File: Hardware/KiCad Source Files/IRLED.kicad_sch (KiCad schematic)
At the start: 14 parts

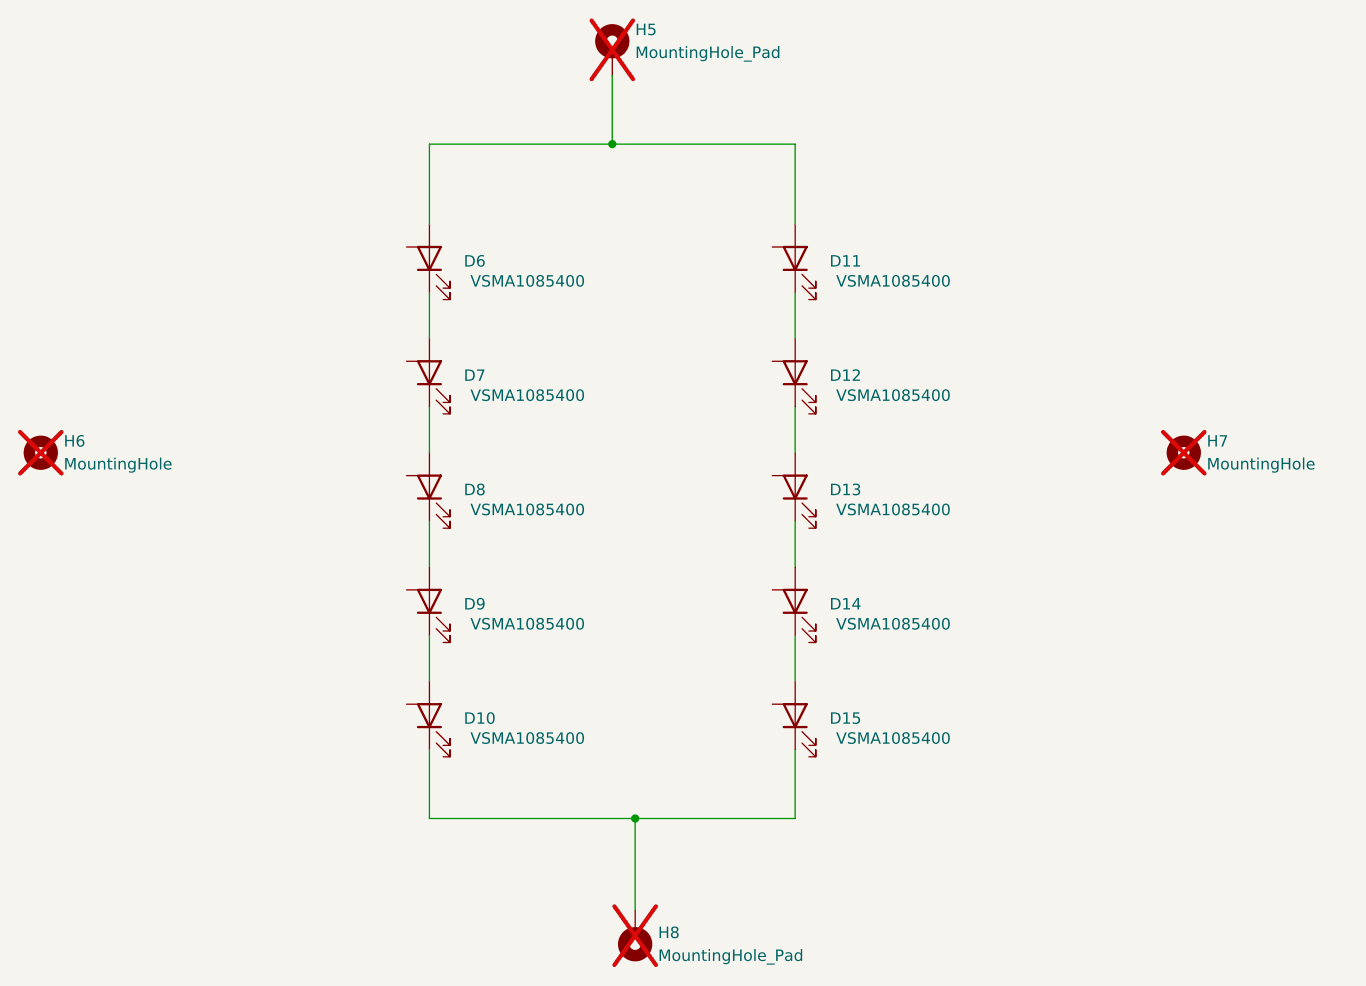
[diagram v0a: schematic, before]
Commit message: V3 connector board: strobe pulse limiter, USB-C fixes, boost protection
Mechanical: board outline, all mounting/tab/breakaway holes and every
existing part position are unchanged (checked against the previous revision);
all new parts are on the top side and no taller than existing parts.
PiTrac software compatibility: the LED current-control circuit and the
DAC/ADC/DIAG interface used by strobe_calibration_manager.py are unchanged.

Strobe (CC Sink sheet)
- AC-coupled pulse limiter: TRIG (DIAG/MOSI via D3/D4) -> C16 220nF ->
  GATE-DRV, R28 10K to GND (tau 2.2 ms). 8.7-130 us strobes and the
  calibration pulse pass (guaranteed >= ~0.38 ms by the MCP1407 input
  limits); a stuck-high DIAG turns the driver off after ~1.7 ms typical,
  <= ~2.8 ms worst case, so 10 A can no longer be held on.

USB-C (Connectors sheet, USB4085-GF-A footprint)
- J2/J5 feed 5 V to the Pis: add 10K Rp on CC1/CC2 (R24-R27, 1206).
- Footprint rebuilt to GCT's land pattern (16 plated 0.40/0.66 mm pins).
  The old VBUS/GND pads had 0.1 mm top-side copper (annular-ring DRC
  errors; Pi supply current only reached them via the barrel/bottom pad).

Boost (Power sheet)
- F1 MF-MSMF050-2 polyfuse in the boost input only (+5V_BST: C1/C2/C3/R1/
  U1); PCB: +5V_BST F.Cu island, +5V B.Cu bridge keeps the Pi feed width.
- D16 P4SMA39CA clamp on VIR (open-feedback fault; relies on F1).
- R5 2K49 -> 10K (was ~0.45 W in a 1/4 W resistor).

Housekeeping
- Project sym/fp-lib-tables; USB4085-GF-A added to the symbol library;
  pin types for custom parts; locally modified Q_NPN/Q_NMOS/LED moved into
  the project library (Q_NPN_EBC, Q_NMOS_SGD, LED_ThermalPad) to keep their
  numeric pinouts; no-connect flags; PWR_FLAGs; GATE-DRV wire to Q3 fixed.
- ERC pin map (project-wide): open emitter on a power rail allowed
  (MC33063 SwE to GND).
- Add V3 Connector Only.kicad_pro (board had no rules; DRC used defaults).
- Breakaway holes marked board-only.
- Regenerated Gerber/drill zips, BOM and centroid CSVs (same for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
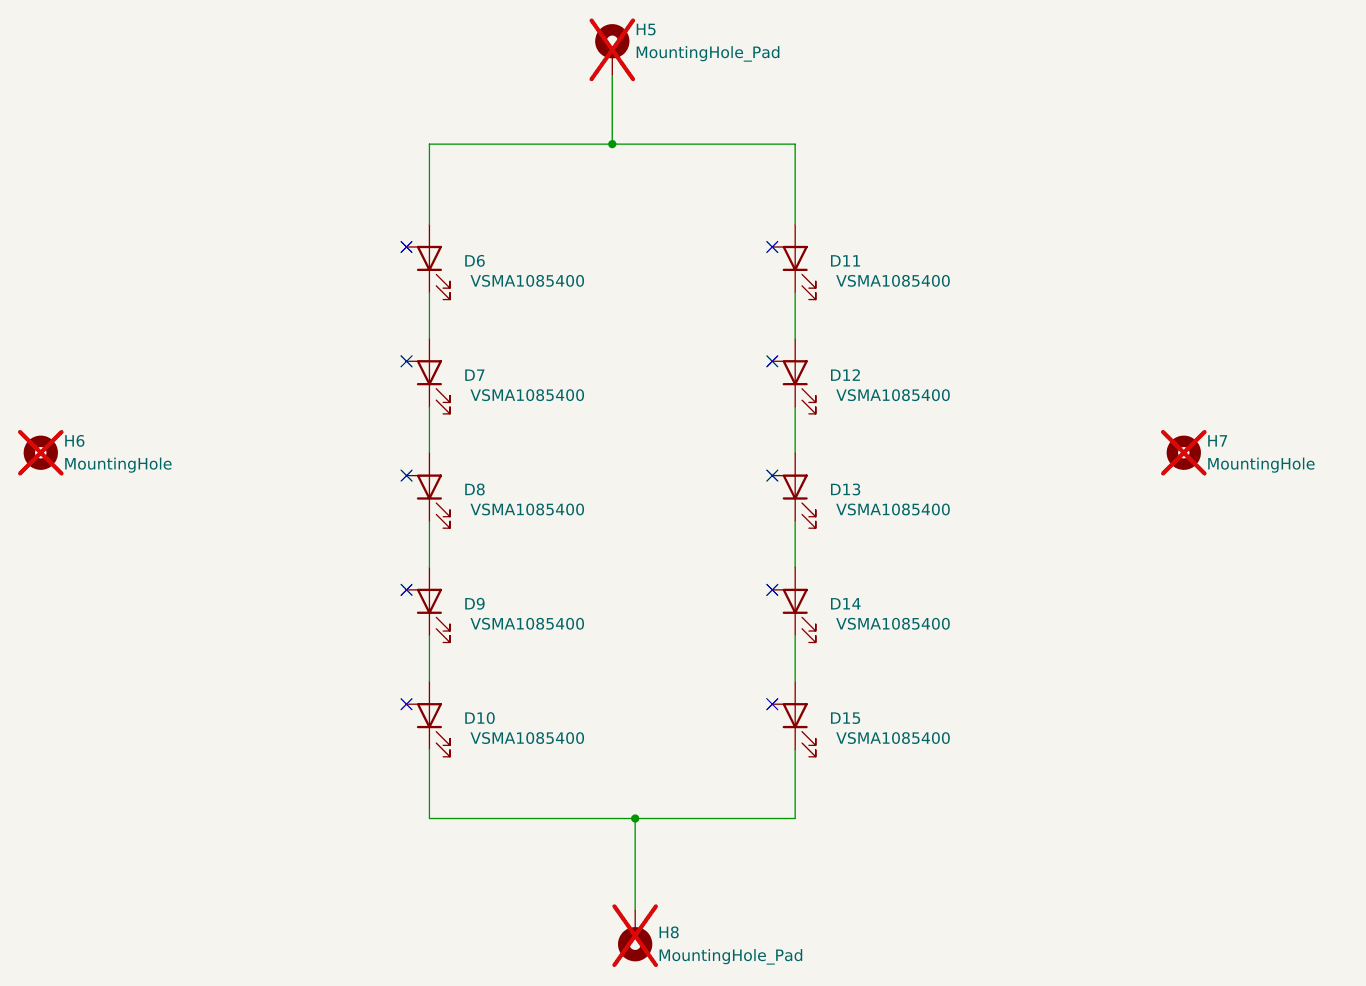
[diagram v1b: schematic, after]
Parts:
- D10, D11, D12, D13, D14, D15, D6, D7, D8, D9: symbol Device:LED -> Pi Connector Parts:LED_ThermalPad
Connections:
- no-connect marks 0 -> 10
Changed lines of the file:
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@@
 	)
 	(symbol
-		(lib_id "Device:LED")
+		(lib_id "Pi Connector Parts:LED_ThermalPad")
 		(at 115.57 120.65 90)
 		(unit 1)
@@
 	)
 	(symbol
-		(lib_id "Device:LED")
+		(lib_id "Pi Connector Parts:LED_ThermalPad")
 		(at 156.21 69.85 90)
 		(unit 1)
@@
 	)
 	(symbol
-		(lib_id "Device:LED")
+		(lib_id "Pi Connector Parts:LED_ThermalPad")
 		(at 156.21 120.65 90)
 		(unit 1)
@@
 	)
 	(symbol
-		(lib_id "Device:LED")
+		(lib_id "Pi Connector Parts:LED_ThermalPad")
 		(at 115.57 69.85 90)
 		(unit 1)
@@
 	)
 	(symbol
-		(lib_id "Device:LED")
+		(lib_id "Pi Connector Parts:LED_ThermalPad")
 		(at 156.21 107.95 90)
 		(unit 1)
@@
 	)
 	(symbol
-		(lib_id "Device:LED")
+		(lib_id "Pi Connector Parts:LED_ThermalPad")
 		(at 115.57 107.95 90)
 		(unit 1)
@@
 	)
 	(symbol
-		(lib_id "Device:LED")
+		(lib_id "Pi Connector Parts:LED_ThermalPad")
 		(at 156.21 95.25 90)
 		(unit 1)
@@
 	)
 	(symbol
-		(lib_id "Device:LED")
+		(lib_id "Pi Connector Parts:LED_ThermalPad")
 		(at 115.57 95.25 90)
 		(unit 1)
@@
 	)
 	(symbol
-		(lib_id "Device:LED")
+		(lib_id "Pi Connector Parts:LED_ThermalPad")
 		(at 115.57 82.55 90)
 		(unit 1)
@@
 	)
 	(symbol
-		(lib_id "Device:LED")
+		(lib_id "Pi Connector Parts:LED_ThermalPad")
 		(at 156.21 82.55 90)
 		(unit 1)
@@
 		)
 	)
+	(no_connect
+		(at 113.03 119.38)
+	)
+	(no_connect
+		(at 153.67 68.58)
+	)
+	(no_connect
+		(at 153.67 119.38)
+	)
+	(no_connect
+		(at 113.03 68.58)
+	)
+	(no_connect
+		(at 153.67 106.68)
+	)
+	(no_connect
+		(at 113.03 106.68)
+	)
+	(no_connect
+		(at 153.67 93.98)
+	)
+	(no_connect
+		(at 113.03 93.98)
+	)
+	(no_connect
+		(at 113.03 81.28)
+	)
+	(no_connect
+		(at 153.67 81.28)
+	)
 )

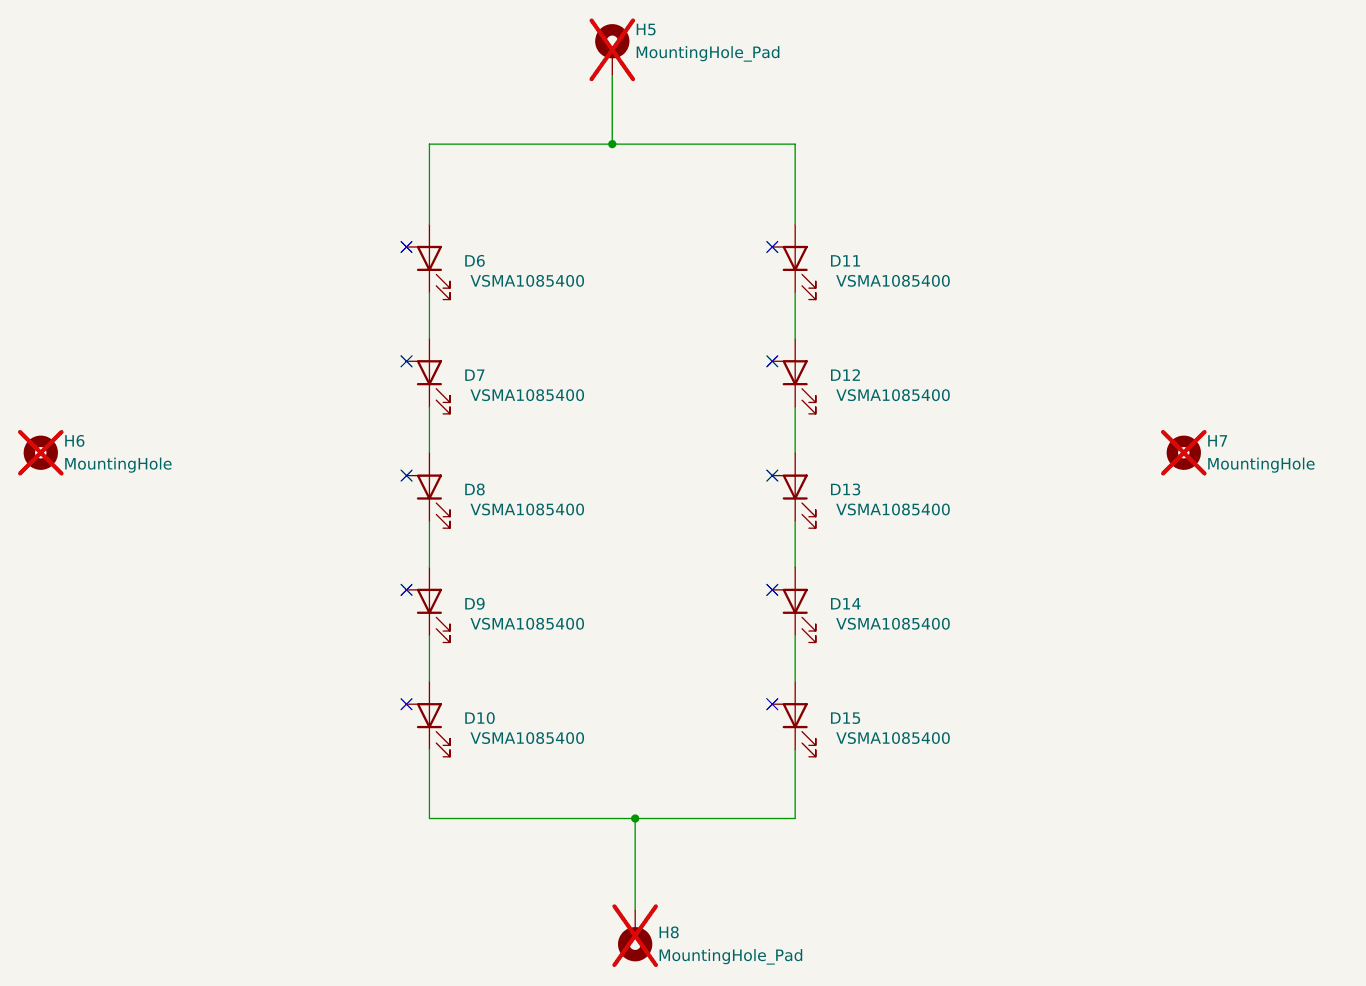
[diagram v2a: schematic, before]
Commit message: IR LEDs: connect the VSMA1085400 center pad (second anode) on both LED boards
Vishay's package drawing (doc 80294) labels the VSMA1085400 pads Anode,
Anode, Cathode; the wide center pad under the die is an anode contact, not
an isolated thermal pad. The LED symbol was inherited from the earlier
Luminus SST-10-IRD (whose center pad is isolated), so pad 3 was left on an
isolated copper island and all strobe current went through the 0.35 mm
outer anode pad.

- Symbol: LED_ThermalPad -> VSMA1085400 (pin 3 named A, Vishay datasheet,
  description). D6-D15 pin 3 wired to pin 2; no-connect markers removed.
- PCB (IRLED Only, and the LED tab of V3 Connector + IRLED): pad 3 on the
  LED's anode net with a 2 mm bridge to pad 2. The gap to the cathode pad
  stays 0.3 mm. LED positions, holes and outline unchanged.
- Two anode nets were auto-renamed by the schematic (Net-(D11-A) ->
  Net-(D11-A-Pad2), Net-(D10-A) -> Net-(D9-K)); pours/pads renamed to match.
- Regenerated IRLED2 Only and V3 Connector + IRLED2 Gerbers and the
  schematic PDF (BOM/centroid unchanged).

ERC 0 (1 intended exclusion). DRC all three boards: 0 errors.

Co-Authored-By: Claude Opus 5.5 <noreply@anthropic.com>
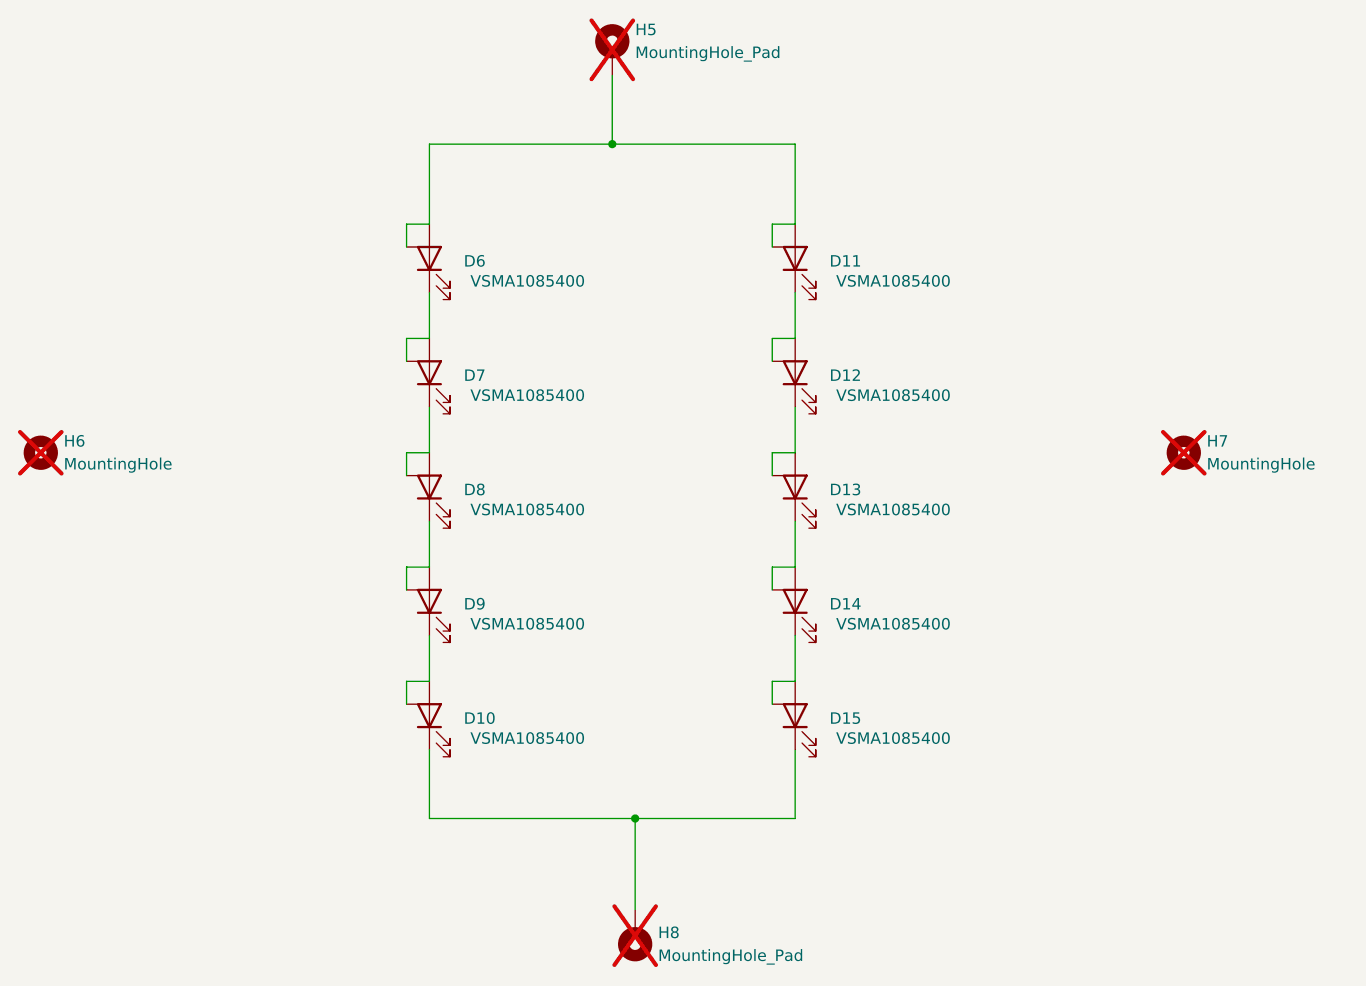
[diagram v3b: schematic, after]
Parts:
- D10, D11, D12, D13, D14, D15, D6, D7, D8, D9: symbol Pi Connector Parts:LED_ThermalPad -> Pi Connector Parts:VSMA1085400
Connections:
- net at D10.2 (A), D9.1 (K): now also D10.3 (A)
- net at D11.1 (K), D12.2 (A): now also D12.3 (A)
- net at D11.2 (A), D6.2 (A), H5.1: now also D11.3 (A), D6.3 (A)
- net at D14.1 (K), D15.2 (A): now also D15.3 (A)
- net at D6.1 (K), D7.2 (A): now also D7.3 (A)
- net at D13.1 (K), D14.2 (A): now also D14.3 (A)
- net at D8.1 (K), D9.2 (A): now also D9.3 (A)
- net at D12.1 (K), D13.2 (A): now also D13.3 (A)
- net at D7.1 (K), D8.2 (A): now also D8.3 (A)
- no-connect marks 10 -> 0
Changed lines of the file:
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@@
 	)
 	(symbol
-		(lib_id "Pi Connector Parts:LED_ThermalPad")
+		(lib_id "Pi Connector Parts:VSMA1085400")
 		(at 115.57 120.65 90)
 		(unit 1)
@@
 	)
 	(symbol
-		(lib_id "Pi Connector Parts:LED_ThermalPad")
+		(lib_id "Pi Connector Parts:VSMA1085400")
 		(at 156.21 69.85 90)
 		(unit 1)
@@
 	)
 	(symbol
-		(lib_id "Pi Connector Parts:LED_ThermalPad")
+		(lib_id "Pi Connector Parts:VSMA1085400")
 		(at 156.21 120.65 90)
 		(unit 1)
@@
 	)
 	(symbol
-		(lib_id "Pi Connector Parts:LED_ThermalPad")
+		(lib_id "Pi Connector Parts:VSMA1085400")
 		(at 115.57 69.85 90)
 		(unit 1)
@@
 	)
 	(symbol
-		(lib_id "Pi Connector Parts:LED_ThermalPad")
+		(lib_id "Pi Connector Parts:VSMA1085400")
 		(at 156.21 107.95 90)
 		(unit 1)
@@
 	)
 	(symbol
-		(lib_id "Pi Connector Parts:LED_ThermalPad")
+		(lib_id "Pi Connector Parts:VSMA1085400")
 		(at 115.57 107.95 90)
 		(unit 1)
@@
 	)
 	(symbol
-		(lib_id "Pi Connector Parts:LED_ThermalPad")
+		(lib_id "Pi Connector Parts:VSMA1085400")
 		(at 156.21 95.25 90)
 		(unit 1)
@@
 	)
 	(symbol
-		(lib_id "Pi Connector Parts:LED_ThermalPad")
+		(lib_id "Pi Connector Parts:VSMA1085400")
 		(at 115.57 95.25 90)
 		(unit 1)
@@
 	)
 	(symbol
-		(lib_id "Pi Connector Parts:LED_ThermalPad")
+		(lib_id "Pi Connector Parts:VSMA1085400")
 		(at 115.57 82.55 90)
 		(unit 1)
@@
 	)
 	(symbol
-		(lib_id "Pi Connector Parts:LED_ThermalPad")
+		(lib_id "Pi Connector Parts:VSMA1085400")
 		(at 156.21 82.55 90)
 		(unit 1)
@@
 		)
 	)
-	(no_connect
-		(at 113.03 119.38)
-	)
-	(no_connect
-		(at 153.67 68.58)
-	)
-	(no_connect
-		(at 153.67 119.38)
-	)
-	(no_connect
-		(at 113.03 68.58)
-	)
-	(no_connect
-		(at 153.67 106.68)
-	)
-	(no_connect
-		(at 113.03 106.68)
-	)
-	(no_connect
-		(at 153.67 93.98)
-	)
-	(no_connect
-		(at 113.03 93.98)
-	)
-	(no_connect
-		(at 113.03 81.28)
-	)
-	(no_connect
-		(at 153.67 81.28)
+	(wire
+		(pts
+			(xy 113.03 119.38) (xy 113.03 116.84)
+		)
+		(stroke
+			(width 0)
+			(type default)
+		)
+	)
+	(wire
+		(pts
+			(xy 113.03 116.84) (xy 115.57 116.84)
+		)
+		(stroke
+			(width 0)
+			(type default)
+		)
+	)
+	(wire
+		(pts
+			(xy 153.67 68.58) (xy 153.67 66.04)
+		)
+		(stroke
+			(width 0)
+			(type default)
+		)
+	)
+	(wire
+		(pts
+			(xy 153.67 66.04) (xy 156.21 66.04)
+		)
+		(stroke
+			(width 0)
+			(type default)
+		)
+	)
+	(wire
+		(pts
+			(xy 153.67 119.38) (xy 153.67 116.84)
+		)
+		(stroke
+			(width 0)
+			(type default)
+		)
+	)
+	(wire
+		(pts
+			(xy 153.67 116.84) (xy 156.21 116.84)
+		)
+		(stroke
+			(width 0)
+			(type default)
+		)
+	)
+	(wire
+		(pts
+			(xy 113.03 68.58) (xy 113.03 66.04)
+		)
+		(stroke
+			(width 0)
+			(type default)
+		)
+	)
+	(wire
+		(pts
+			(xy 113.03 66.04) (xy 115.57 66.04)
+		)
+		(stroke
+			(width 0)
+			(type default)
+		)
+	)
+	(wire
+		(pts
+			(xy 153.67 106.68) (xy 153.67 104.14)
+		)
+		(stroke
+			(width 0)
+			(type default)
+		)
+	)
+	(wire
+		(pts
+			(xy 153.67 104.14) (xy 156.21 104.14)
+		)
+		(stroke
+			(width 0)
+			(type default)
+		)
+	)
+	(wire
+		(pts
+			(xy 113.03 106.68) (xy 113.03 104.14)
+		)
+		(stroke
+			(width 0)
+			(type default)
+		)
+	)
+	(wire
+		(pts
+			(xy 113.03 104.14) (xy 115.57 104.14)
+		)
+		(stroke
+			(width 0)
+			(type default)
+		)
+	)
+	(wire
+		(pts
+			(xy 153.67 93.98) (xy 153.67 91.44)
+		)
+		(stroke
+			(width 0)
+			(type default)
+		)
+	)
+	(wire
+		(pts
+			(xy 153.67 91.44) (xy 156.21 91.44)
+		)
+		(stroke
+			(width 0)
+			(type default)
+		)
+	)
+	(wire
+		(pts
+			(xy 113.03 93.98) (xy 113.03 91.44)
+		)
+		(stroke
+			(width 0)
+			(type default)
+		)
+	)
+	(wire
+		(pts
+			(xy 113.03 91.44) (xy 115.57 91.44)
+		)
+		(stroke
+			(width 0)
+			(type default)
+		)
+	)
+	(wire
+		(pts
+			(xy 113.03 81.28) (xy 113.03 78.74)
+		)
+		(stroke
+			(width 0)
+			(type default)
+		)
+	)
+	(wire
+		(pts
+			(xy 113.03 78.74) (xy 115.57 78.74)
+		)
+		(stroke
+			(width 0)
+			(type default)
+		)
+	)
+	(wire
+		(pts
+			(xy 153.67 81.28) (xy 153.67 78.74)
+		)
+		(stroke
+			(width 0)
+			(type default)
+		)
+	)
+	(wire
+		(pts
+			(xy 153.67 78.74) (xy 156.21 78.74)
+		)
+		(stroke
+			(width 0)
+			(type default)
+		)
 	)
 )
